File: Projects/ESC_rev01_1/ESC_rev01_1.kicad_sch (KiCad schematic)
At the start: 0 parts

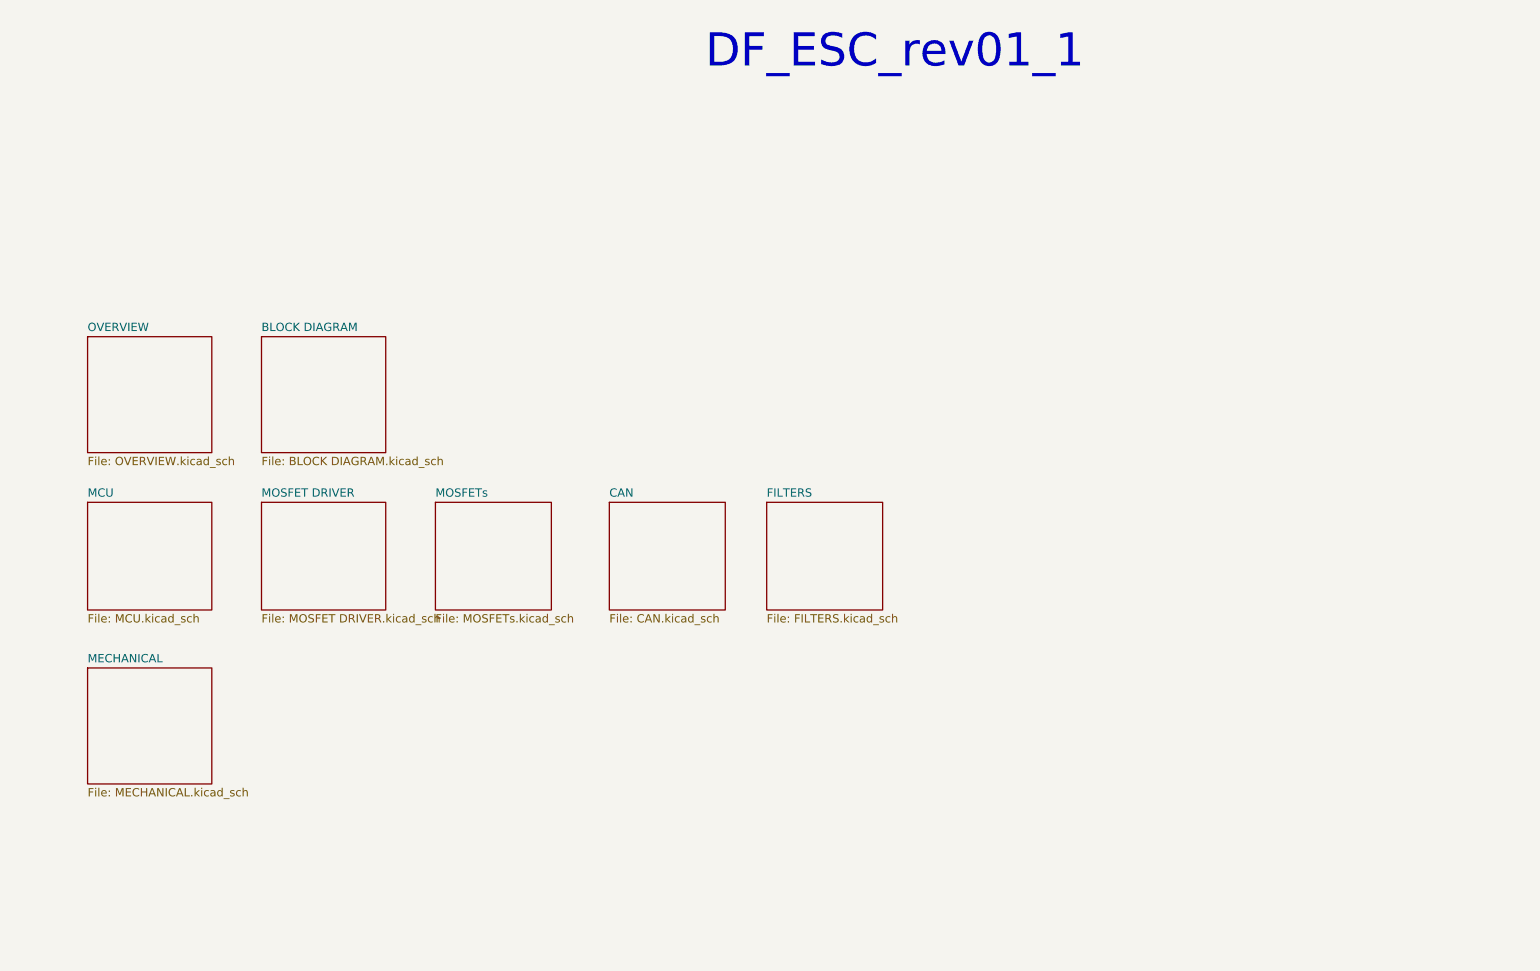
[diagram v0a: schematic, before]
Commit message: Update 07
Schematic is ready
INPUT PROTECTION schematic created
MOSFETs schematic created
CAN schematic created
FILTERs schematic created
MECHANICAL schematic created
STEP-DOWN schematic created
Footprints, 3D models are added and corrected (major issues)
Component placement started
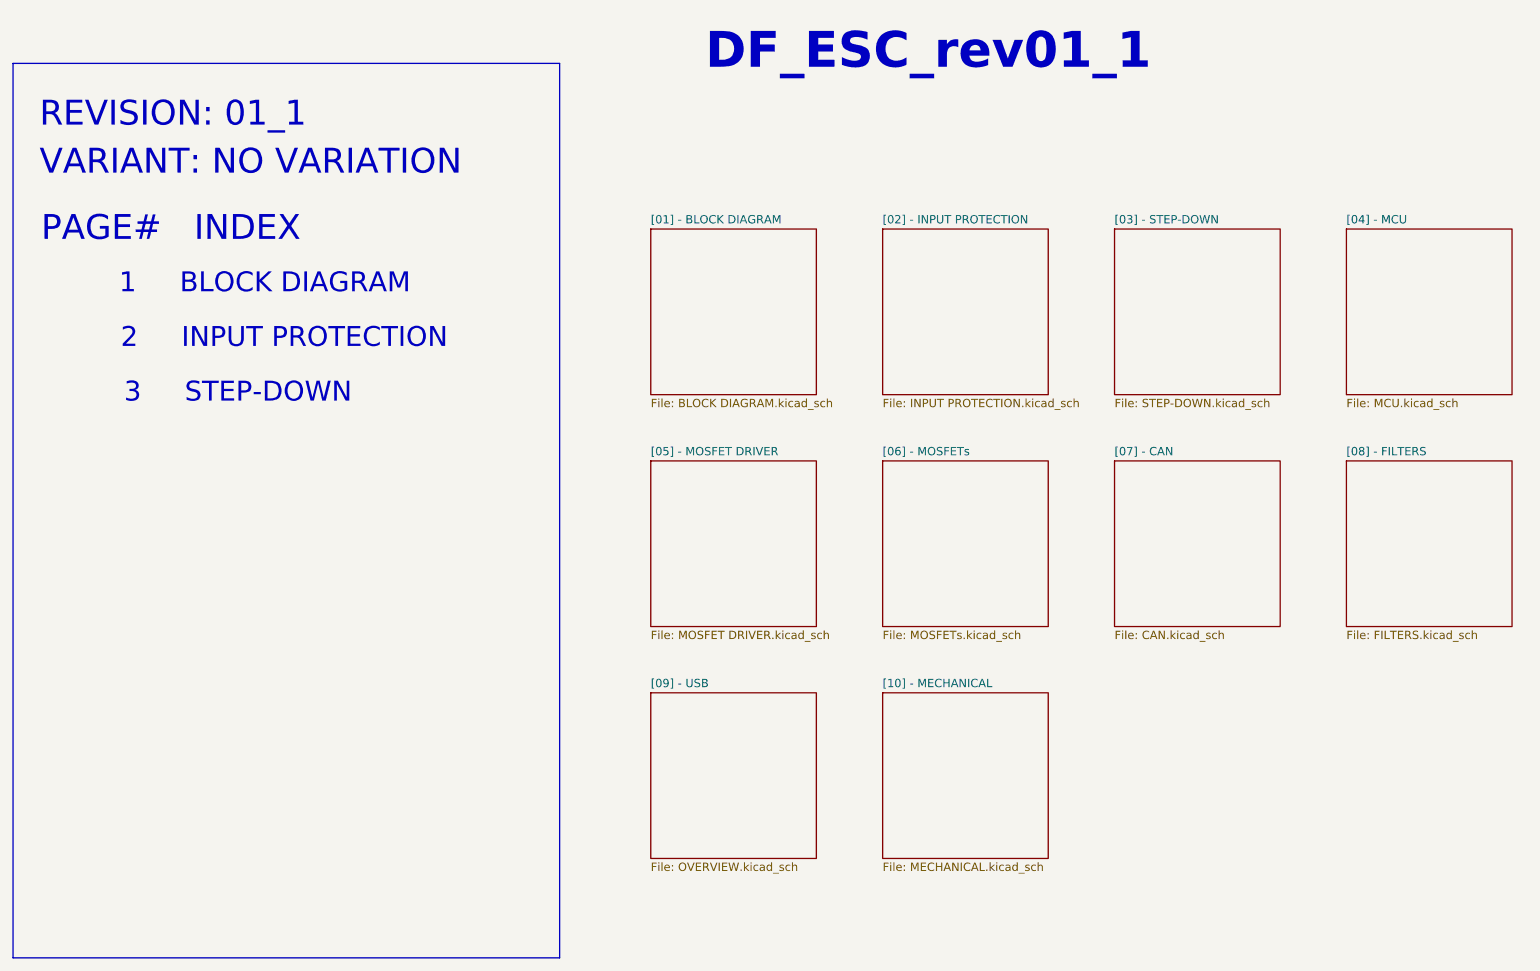
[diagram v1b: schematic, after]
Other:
- sheet BLOCK DIAGRAM renamed [01] - BLOCK DIAGRAM
- sheet CAN renamed [07] - CAN
- sheet FILTERS renamed [08] - FILTERS
- sheet MCU renamed [04] - MCU
- sheet MECHANICAL renamed [10] - MECHANICAL
- sheet MOSFET DRIVER renamed [05] - MOSFET DRIVER
- sheet MOSFETs renamed [06] - MOSFETs
- sheet OVERVIEW renamed [09] - USB
- added sheet [02] - INPUT PROTECTION (INPUT PROTECTION.kicad_sch)
- added sheet [03] - STEP-DOWN (STEP-DOWN.kicad_sch)
- note added: "1 BLOCK DIAGRAM"
- note added: "2 INPUT PROTECTION"
- note added: "3 STEP-DOWN"
- note added: "PAGE# INDEX"
- note added: "REVISION: 01_1"
- note added: "VARIANT: NO VARIATION"

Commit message: Update 08
Component placement is almost done
Check one more time and correct if needed
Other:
- note added: "10 MECHANICAL"
- note added: "4 MCU"
- note added: "5 MOSFET DRIVER"
- note added: "6 MOSFETs"
- note added: "7 CAN"
- note added: "8 FILTERs"
- note added: "9 USB"
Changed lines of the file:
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@@
+		)
+	)
+	(text "5     MOSFET DRIVER"
+		(exclude_from_sim no)
+		(at 34.29 86.36 0)
+		(effects
+			(font
+				(size 3.048 3.048)
+				(thickness 0.5625)
+			)
+			(justify left)
+		)
+	)
+	(text "6     MOSFETs"
+		(exclude_from_sim no)
+		(at 34.29 94.488 0)
+		(effects
+			(font
+				(size 3.048 3.048)
+				(thickness 0.5625)
+			)
+			(justify left)
 		)
 	)
@@
 		)
 	)
+	(text "8     FILTERs"
+		(exclude_from_sim no)
+		(at 34.544 110.998 0)
+		(effects
+			(font
+				(size 3.048 3.048)
+				(thickness 0.5625)
+			)
+			(justify left)
+		)
+	)
+	(text "10     MECHANICAL"
+		(exclude_from_sim no)
+		(at 32.258 126.746 0)
+		(effects
+			(font
+				(size 3.048 3.048)
+				(thickness 0.5625)
+			)
+			(justify left)
+		)
+	)
 	(text "2     INPUT PROTECTION"
 		(exclude_from_sim no)
-		(at 34.29 62.484 0)
+		(at 34.036 62.23 0)
 		(effects
 			(font
@@
 	(text "3     STEP-DOWN"
 		(exclude_from_sim no)
-		(at 34.798 70.866 0)
+		(at 34.036 70.358 0)
 		(effects
 			(font
@@
 		(exclude_from_sim no)
 		(at 34.036 54.102 0)
+		(effects
+			(font
+				(size 3.048 3.048)
+				(thickness 0.5625)
+			)
+			(justify left)
+		)
+	)
+	(text "7     CAN"
+		(exclude_from_sim no)
+		(at 34.29 103.124 0)
+		(effects
+			(font
+				(size 3.048 3.048)
+				(thickness 0.5625)
+			)
+			(justify left)
+		)
+	)
+	(text "4     MCU"
+		(exclude_from_sim no)
+		(at 34.29 78.232 0)
 		(effects
 			(font
@@
 			)
 			(justify left)
+		)
+	)
+	(text "9     USB"
+		(exclude_from_sim no)
+		(at 34.544 119.126 0)
+		(effects
+			(font
+				(size 3.048 3.048)
+				(thickness 0.5625)
+			)
+			(justify left)
